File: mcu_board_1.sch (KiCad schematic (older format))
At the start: 19 parts, among them J1 Conn_01x03, SW1 SW_SPST, U1 STM32G474QET6, Y1 32.7680kHz, Y2 10MHz

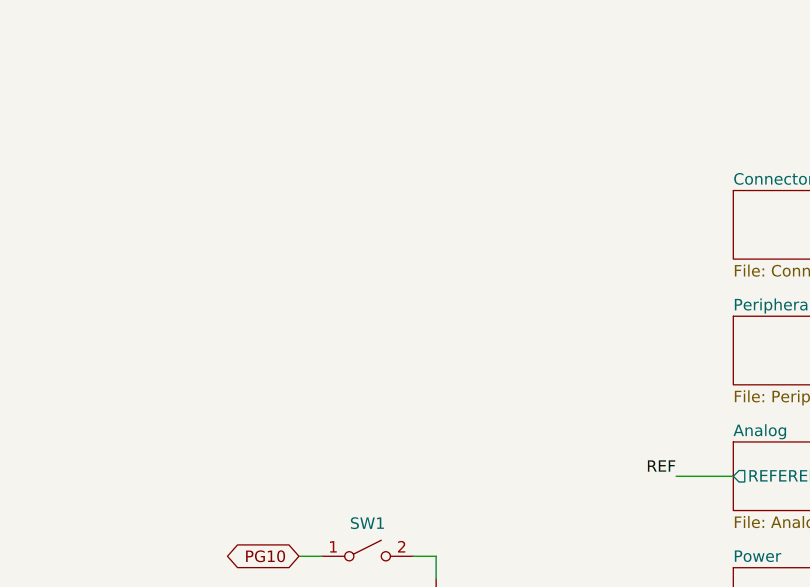
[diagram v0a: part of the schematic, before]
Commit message: MCU prepped for fanout
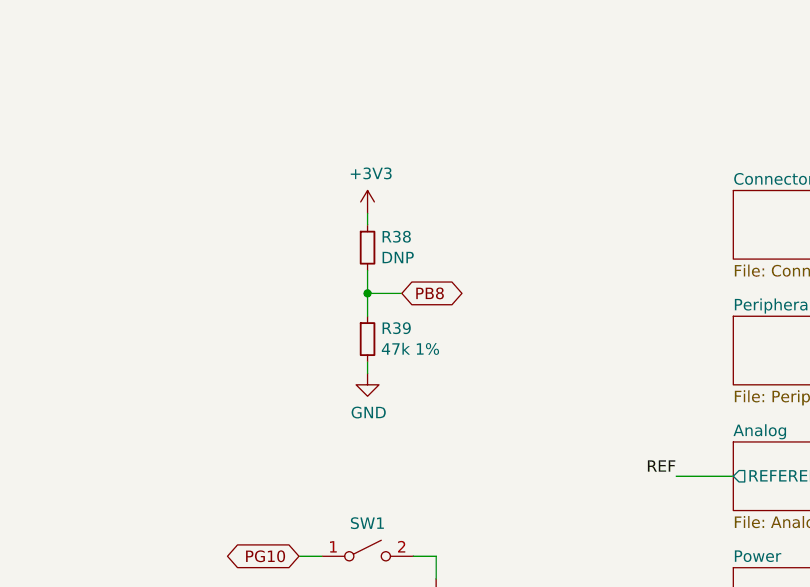
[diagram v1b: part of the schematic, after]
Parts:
- added R38: DNP, Resistor_SMD:R_0603_1608Metric_Pad1.05x0.95mm_HandSolder, symbol Device:R_Small
- added R39: 47k 1%, Resistor_SMD:R_0603_1608Metric_Pad1.05x0.95mm_HandSolder, symbol Device:R_Small
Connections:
- net +3V3: now also R38.1
- net GND: now also R39.2
- net PB8: now also R38.2, R39.1
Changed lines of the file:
@@
 Wire Wire Line
 	7800 5200 7900 5200
+Text GLabel 8250 4050 2    50   BiDi ~ 0
+PB8
+$Comp
+L Device:R_Small R39
+U 1 1 5FBA5C60
+P 8100 4250
+F 0 "R39" H 8159 4296 50  0000 L CNN
+F 1 "47k 1%" H 8159 4205 50  0000 L CNN
+F 2 "Resistor_SMD:R_0603_1608Metric_Pad1.05x0.95mm_HandSolder" H 8100 4250 50  0001 C CNN
+F 3 "~" H 8100 4250 50  0001 C CNN
+	1    8100 4250
+	1    0    0    -1
+$EndComp
+$Comp
+L Device:R_Small R38
+U 1 1 5FBA6B17
+P 8100 3850
+F 0 "R38" H 8159 3896 50  0000 L CNN
+F 1 "DNP" H 8159 3805 50  0000 L CNN
+F 2 "Resistor_SMD:R_0603_1608Metric_Pad1.05x0.95mm_HandSolder" H 8100 3850 50  0001 C CNN
+F 3 "~" H 8100 3850 50  0001 C CNN
+	1    8100 3850
+	1    0    0    -1
+$EndComp
+$Comp
+L power:GND #PWR0109
+U 1 1 5FBA73BD
+P 8100 4400
+F 0 "#PWR0109" H 8100 4150 50  0001 C CNN
+F 1 "GND" H 8105 4227 50  0000 C CNN
+F 2 "" H 8100 4400 50  0001 C CNN
+F 3 "" H 8100 4400 50  0001 C CNN
+	1    8100 4400
+	1    0    0    -1
+$EndComp
+$Comp
+L power:+3V3 #PWR0108
+U 1 1 5FBA7E65
+P 8100 3700
+F 0 "#PWR0108" H 8100 3550 50  0001 C CNN
+F 1 "+3V3" H 8115 3873 50  0000 C CNN
+F 2 "" H 8100 3700 50  0001 C CNN
+F 3 "" H 8100 3700 50  0001 C CNN
+	1    8100 3700
+	1    0    0    -1
+$EndComp
+Wire Wire Line
+	8100 3950 8100 4050
+Wire Wire Line
+	8100 4400 8100 4350
+Wire Wire Line
+	8100 3750 8100 3700
+Wire Wire Line
+	8250 4050 8100 4050
+Connection ~ 8100 4050
+Wire Wire Line
+	8100 4050 8100 4150
 $EndSCHEMATC

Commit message: done and done
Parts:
- added C36: 100n, Capacitor_SMD:C_0603_1608Metric_Pad1.05x0.95mm_HandSolder, symbol Device:C_Small
- added C37: 1U, Capacitor_SMD:C_0603_1608Metric_Pad1.05x0.95mm_HandSolder, symbol Device:C_Small
- added H1, H2, H3, H4: MountingHole_Pad, MountingHole:MountingHole_3.2mm_M3_Pad_Via, symbol Mechanical:MountingHole_Pad
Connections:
- net GNDA is gone; now on net GND: C6.1, U1.42 (VSSA)
- net GND: now also J1.3 (Pin_3), C36.1, C37.1, H1.1, H2.1, H3.1, H4.1; no longer J1.2 (Pin_2)
- net PG10: now also C36.2
- net REF: now also C37.2
- net at C5.2, U1.6 (VBAT): now also J1.2 (Pin_2); no longer J1.3 (Pin_3)
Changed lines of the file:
@@
 U 1 1 5FA2BF42
 P 1650 2050
-F 0 "J1" V 1568 1862 50  0000 R CNN
+F 0 "J1" V 1750 2050 50  0000 R CNN
 F 1 "Conn_01x03" V 1523 1862 50  0001 R CNN
 F 2 "Connector_PinHeader_2.54mm:PinHeader_1x03_P2.54mm_Vertical" H 1650 2050 50  0001 C CNN
@@
 L power:GND #PWR05
 U 1 1 5FA2E3B6
-P 1650 2300
-F 0 "#PWR05" H 1650 2050 50  0001 C CNN
-F 1 "GND" H 1650 2150 50  0000 C CNN
-F 2 "" H 1650 2300 50  0001 C CNN
-F 3 "" H 1650 2300 50  0001 C CNN
-	1    1650 2300
-	1    0    0    -1
-$EndComp
-Wire Wire Line
-	1650 2300 1650 2250
+P 2050 2150
+F 0 "#PWR05" H 2050 1900 50  0001 C CNN
+F 1 "GND" H 2050 2000 50  0000 C CNN
+F 2 "" H 2050 2150 50  0001 C CNN
+F 3 "" H 2050 2150 50  0001 C CNN
+	1    2050 2150
+	1    0    0    -1
+$EndComp
 Wire Wire Line
 	1750 2950 1750 2650
@@
 Wire Wire Line
 	1600 2650 1750 2650
-Connection ~ 1750 2650
-Wire Wire Line
-	1750 2650 1750 2250
 $Comp
 L power:GND #PWR04
@@
 Text Label 3450 6600 1    50   ~ 0
 REF
-Text Label 9450 4850 2    50   ~ 0
+Text Label 9050 4850 2    50   ~ 0
 REF
-$Comp
-L power:GNDA #PWR012
-U 1 1 5FA78748
-P 3150 6850
-F 0 "#PWR012" H 3150 6600 50  0001 C CNN
-F 1 "GNDA" H 3155 6677 50  0000 C CNN
-F 2 "" H 3150 6850 50  0001 C CNN
-F 3 "" H 3150 6850 50  0001 C CNN
-	1    3150 6850
-	1    0    0    -1
-$EndComp
 $Comp
 L power:+3.3VA #PWR013
@@
 $EndComp
 Wire Wire Line
-	9450 4850 9700 4850
+	9050 4850 9200 4850
 $Comp
 L Switch:SW_SPST SW?
@@
 L power:GND #PWR024
 U 1 1 601B9E39
-P 8400 5300
-F 0 "#PWR024" H 8400 5050 50  0001 C CNN
-F 1 "GND" H 8405 5127 50  0000 C CNN
-F 2 "" H 8400 5300 50  0001 C CNN
-F 3 "" H 8400 5300 50  0001 C CNN
-	1    8400 5300
+P 8400 5650
+F 0 "#PWR024" H 8400 5400 50  0001 C CNN
+F 1 "GND" H 8405 5477 50  0000 C CNN
+F 2 "" H 8400 5650 50  0001 C CNN
+F 3 "" H 8400 5650 50  0001 C CNN
+	1    8400 5650
 	1    0    0    -1
 $EndComp
@@
 	8300 5200 8400 5200
 Wire Wire Line
-	8400 5200 8400 5300
-Wire Wire Line
-	7800 5200 7900 5200
+	8400 5200 8400 5650
+Wire Wire Line
+	7800 5200 7850 5200
 Text GLabel 8250 4050 2    50   BiDi ~ 0
 PB8
@@
 Wire Wire Line
 	8100 4050 8100 4150
+$Comp
+L power:GND #PWR0110
+U 1 1 5FADCD14
+P 3150 6850
+F 0 "#PWR0110" H 3150 6600 50  0001 C CNN
+F 1 "GND" H 3155 6677 50  0000 C CNN
+F 2 "" H 3150 6850 50  0001 C CNN
+F 3 "" H 3150 6850 50  0001 C CNN
+	1    3150 6850
+	1    0    0    -1
+$EndComp
+$Comp
+L Mechanical:MountingHole_Pad H1
+U 1 1 5FB10C83
+P 8600 750
+F 0 "H1" H 8700 753 50  0000 L CNN
+F 1 "MountingHole_Pad" H 8700 708 50  0001 L CNN
+F 2 "MountingHole:MountingHole_3.2mm_M3_Pad_Via" H 8600 750 50  0001 C CNN
+F 3 "~" H 8600 750 50  0001 C CNN
+	1    8600 750
+	1    0    0    -1
+$EndComp
+$Comp
+L power:GND #PWR012
+U 1 1 5FB1161E
+P 8600 850
+F 0 "#PWR012" H 8600 600 50  0001 C CNN
+F 1 "GND" H 8605 677 50  0000 C CNN
+F 2 "" H 8600 850 50  0001 C CNN
+F 3 "" H 8600 850 50  0001 C CNN
+	1    8600 850
+	1    0    0    -1
+$EndComp
+$Comp
+L Mechanical:MountingHole_Pad H2
+U 1 1 5FB12685
+P 8950 750
+F 0 "H2" H 9050 753 50  0000 L CNN
+F 1 "MountingHole_Pad" H 9050 708 50  0001 L CNN
+F 2 "MountingHole:MountingHole_3.2mm_M3_Pad_Via" H 8950 750 50  0001 C CNN
+F 3 "~" H 8950 750 50  0001 C CNN
+	1    8950 750
+	1    0    0    -1
+$EndComp
+$Comp
+L power:GND #PWR0111
+U 1 1 5FB1268B
+P 8950 850
+F 0 "#PWR0111" H 8950 600 50  0001 C CNN
+F 1 "GND" H 8955 677 50  0000 C CNN
+F 2 "" H 8950 850 50  0001 C CNN
+F 3 "" H 8950 850 50  0001 C CNN
+	1    8950 850
+	1    0    0    -1
+$EndComp
+$Comp
+L Mechanical:MountingHole_Pad H3
+U 1 1 5FB16D63
+P 9300 750
+F 0 "H3" H 9400 753 50  0000 L CNN
+F 1 "MountingHole_Pad" H 9400 708 50  0001 L CNN
+F 2 "MountingHole:MountingHole_3.2mm_M3_Pad_Via" H 9300 750 50  0001 C CNN
+F 3 "~" H 9300 750 50  0001 C CNN
+	1    9300 750
+	1    0    0    -1
+$EndComp
+$Comp
+L power:GND #PWR0112
+U 1 1 5FB16D69
+P 9300 850
+F 0 "#PWR0112" H 9300 600 50  0001 C CNN
+F 1 "GND" H 9305 677 50  0000 C CNN
+F 2 "" H 9300 850 50  0001 C CNN
+F 3 "" H 9300 850 50  0001 C CNN
+	1    9300 850
+	1    0    0    -1
+$EndComp
+$Comp
+L Mechanical:MountingHole_Pad H4
+U 1 1 5FB1B4FF
+P 9650 750
+F 0 "H4" H 9750 753 50  0000 L CNN
+F 1 "MountingHole_Pad" H 9750 708 50  0001 L CNN
+F 2 "MountingHole:MountingHole_3.2mm_M3_Pad_Via" H 9650 750 50  0001 C CNN
+F 3 "~" H 9650 750 50  0001 C CNN
+	1    9650 750
+	1    0    0    -1
+$EndComp
+$Comp
+L power:GND #PWR0113
+U 1 1 5FB1B505
+P 9650 850
+F 0 "#PWR0113" H 9650 600 50  0001 C CNN
+F 1 "GND" H 9655 677 50  0000 C CNN
+F 2 "" H 9650 850 50  0001 C CNN
+F 3 "" H 9650 850 50  0001 C CNN
+	1    9650 850
+	1    0    0    -1
+$EndComp
+$Comp
+L Device:C_Small C36
+U 1 1 5FBD1086
+P 7850 5500
+F 0 "C36" H 7750 5400 50  0000 C CNN
+F 1 "100n" H 7700 5600 50  0000 C CNN
+F 2 "Capacitor_SMD:C_0603_1608Metric_Pad1.05x0.95mm_HandSolder" H 7850 5500 50  0001 C CNN
+F 3 "~" H 7850 5500 50  0001 C CNN
+	1    7850 5500
+	-1   0    0    1
+$EndComp
+$Comp
+L power:GND #PWR0114
+U 1 1 5FBD215D
+P 7850 5650
+F 0 "#PWR0114" H 7850 5400 50  0001 C CNN
+F 1 "GND" H 7855 5477 50  0000 C CNN
+F 2 "" H 7850 5650 50  0001 C CNN
+F 3 "" H 7850 5650 50  0001 C CNN
+	1    7850 5650
+	1    0    0    -1
+$EndComp
+Wire Wire Line
+	7850 5650 7850 5600
+Wire Wire Line
+	7850 5400 7850 5200
+Connection ~ 7850 5200
+Wire Wire Line
+	7850 5200 7900 5200
+$Comp
+L Device:C_Small C37
+U 1 1 5FBE7EC6
+P 9200 5050
+F 0 "C37" H 9100 4950 50  0000 C CNN
+F 1 "1U" H 9100 5150 50  0000 C CNN
+F 2 "Capacitor_SMD:C_0603_1608Metric_Pad1.05x0.95mm_HandSolder" H 9200 5050 50  0001 C CNN
+F 3 "~" H 9200 5050 50  0001 C CNN
+	1    9200 5050
+	-1   0    0    1
+$EndComp
+$Comp
+L power:GND #PWR0115
+U 1 1 5FBEE59D
+P 9200 5250
+F 0 "#PWR0115" H 9200 5000 50  0001 C CNN
+F 1 "GND" H 9205 5077 50  0000 C CNN
+F 2 "" H 9200 5250 50  0001 C CNN
+F 3 "" H 9200 5250 50  0001 C CNN
+	1    9200 5250
+	1    0    0    -1
+$EndComp
+Wire Wire Line
+	9200 5250 9200 5150
+Wire Wire Line
+	9200 4950 9200 4850
+Connection ~ 9200 4850
+Wire Wire Line
+	9200 4850 9700 4850
+Wire Wire Line
+	1750 2250 1750 2350
+Wire Wire Line
+	1750 2350 1900 2350
+Wire Wire Line
+	1900 2350 1900 2050
+Wire Wire Line
+	1900 2050 2050 2050
+Wire Wire Line
+	2050 2050 2050 2150
+Wire Wire Line
+	1750 2650 1750 2450
+Wire Wire Line
+	1750 2450 1650 2450
+Wire Wire Line
+	1650 2250 1650 2450
+Connection ~ 1750 2650
 $EndSCHEMATC
